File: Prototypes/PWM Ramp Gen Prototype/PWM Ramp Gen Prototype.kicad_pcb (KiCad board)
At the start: 2 copper layers, 115 parts, among them J1 Conn_01x03, J2 Conn_01x03, J3 Conn_01x10, U1 HFBR-2521Z, U10 BD50FC0FP-E2, U11 BD50FC0FP-E2, U12 BD33FC0FP-E2, U13 REF3433TIDBVR, U2 AFBR-1528CZ, U3 74LVC1G97, U4 74LVC1G97, U5 74LV1T04, U6 LT6230, U7 TLV3502, U8 74LVC1G97, U9 AD8602

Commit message: Finishing layout
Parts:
- added kibuzzard-65FA71D7: G***, kibuzzard-65FA71D7, B.Cu at (145.7, 43.4)
- added kibuzzard-65FA722F: G***, kibuzzard-65FA722F, B.Cu at (150.2, 48.5)
- added kibuzzard-65FA7252: G***, kibuzzard-65FA7252, B.Cu at (150.5, 84.8)
- moved TP27 137.6 mm to (108.0, 70.5)
- moved TP3 126.8 mm to (142.0, 57.5)
- moved TP31 121.0 mm to (145.5, 41.5)
- moved TP36 118.6 mm to (152.5, 41.5)
- moved TP30 114.8 mm to (142.0, 54.5)
- moved TP33 111.6 mm to (142.0, 63.5)
- moved J3 104.2 mm to (162.5, 52.1)
- moved R16 34.8 mm to (145.5, 59.0)
- moved TP23 33.6 mm to (145.5, 56.0)
- moved TP22 32.8 mm to (148.5, 68.2)
- moved TP21 30.2 mm to (144.5, 68.2)
- moved R15 28.1 mm to (150.0, 61.5), turned to 90 degrees
- moved U8 27.6 mm to (146.5, 61.5), turned to 180 degrees
- moved R23 26.4 mm to (139.0, 57.5), turned to 90 degrees
- moved R14 26.3 mm to (145.5, 65.0), turned to 90 degrees
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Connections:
- U1 pad 6: unconnected-(U1-MNT-Pad5) -> unconnected-(U1-MNT-Pad6)
- U2 pad 6: unconnected-(U2-MNT-Pad5) -> unconnected-(U2-MNT-Pad6)
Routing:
- net /HALF_V_{REF}: track 0.00 -> 105.9 mm, vias 0 -> 3
- net /Integrator Ramp Generator/V_{SERVO}: track 0.00 -> 74.1 mm, vias 0 -> 2
- net /+5V_ANA: track 0.00 -> 72.5 mm, vias 0 -> 9
- net +3.3V: track 0.00 -> 71.7 mm, vias 0 -> 7
- net +5V: track 0.00 -> 65.7 mm, vias 0 -> 9
- net /RAMP: track 0.00 -> 44.8 mm, vias 0 -> 1
- net /PWM_MIN: track 0.00 -> 39.0 mm, vias 0 -> 1
- net /PWM_MAX: track 0.00 -> 37.0 mm, vias 0 -> 1
- net Net-(D1-K): track 0.00 -> 33.8 mm, vias 0 -> 2
- net /SQUARE_IN: track 0.00 -> 31.6 mm
- net /V_{IN}: track 0.00 -> 20.2 mm, vias 0 -> 1
- net Net-(U7A-+): track 0.00 -> 19.7 mm
- net V_{REF}: track 0.00 -> 19.5 mm, vias 0 -> 4
- net Net-(U7B-+): track 0.00 -> 17.5 mm
- net /Square Wave Input/Y: track 0.00 -> 16.3 mm
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- added copper zone on F.Cu, net +3.3V
- added copper zone on In2.Cu, net +3.3V
- added copper zone on F.Cu, net +5V
- added copper zone on In2.Cu, net +5V
- added copper zone on F.Cu, net /+5V_ANA
- added copper zone on In2.Cu, net /+5V_ANA
- added copper zone on B.Cu, net GND
- added copper zone on F.Cu, net GND
- added copper zone on In1.Cu, net GND
- added copper zone on F.Cu, net Net-(D2-K)
- added copper zone on F.Cu, net Net-(D3-K)
- added copper zone on F.Cu, net Net-(U13-VDD)
- added copper zone on In2.Cu, net V_{REF}
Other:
- board outline added: 67 x 52 mm
- copper layers 2 -> 4
- rule pad_to_mask_clearance: 0 -> 0.0381
- board text added: "+3.3V_{D}"
- board text added: "+5V_{ANA}"
- board text added: "+5V_{D}"
- board text added: "PWM_MAX"
- board text added: "PWM_MIN"
- board text added: "RAMP"
- board text added: "V_{REF}"
- board text added: "V_{REF}/2"

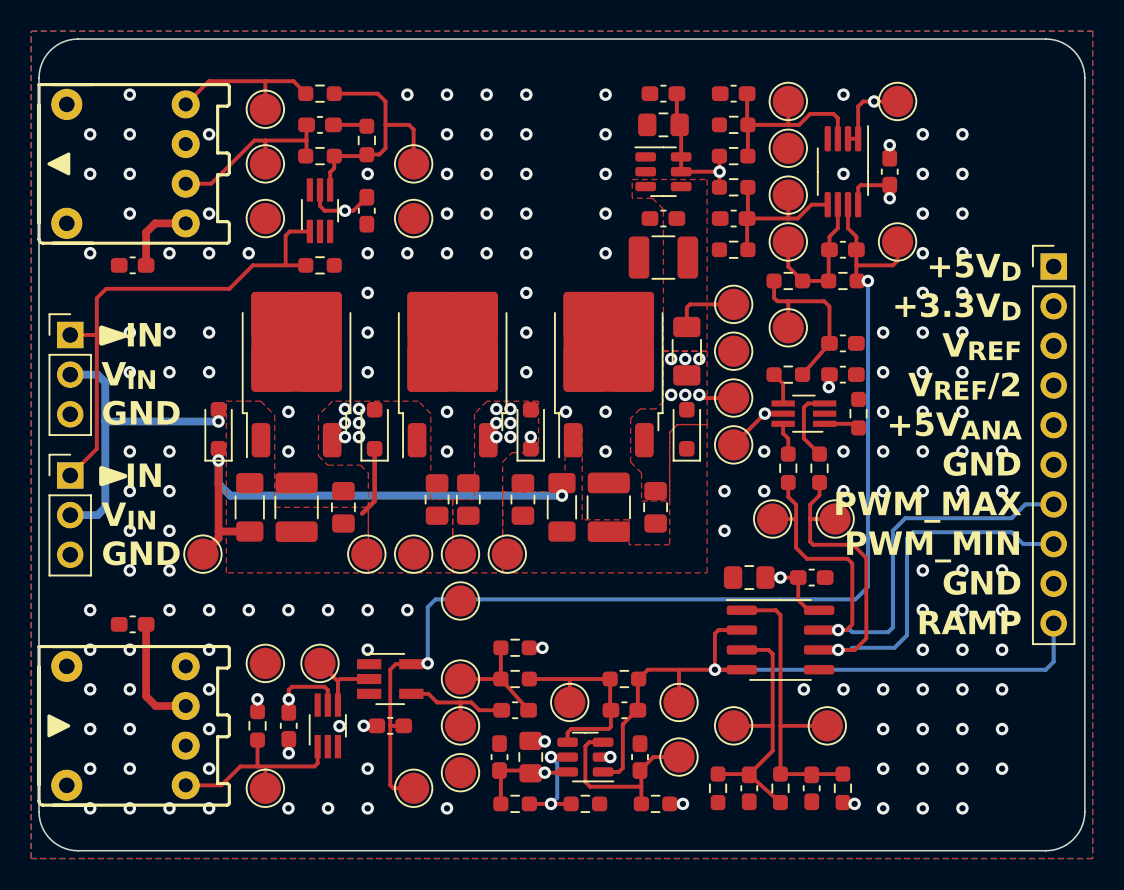
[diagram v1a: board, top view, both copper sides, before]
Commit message: Comparator and Op-amp tweaks for BOM consolidation; final layout
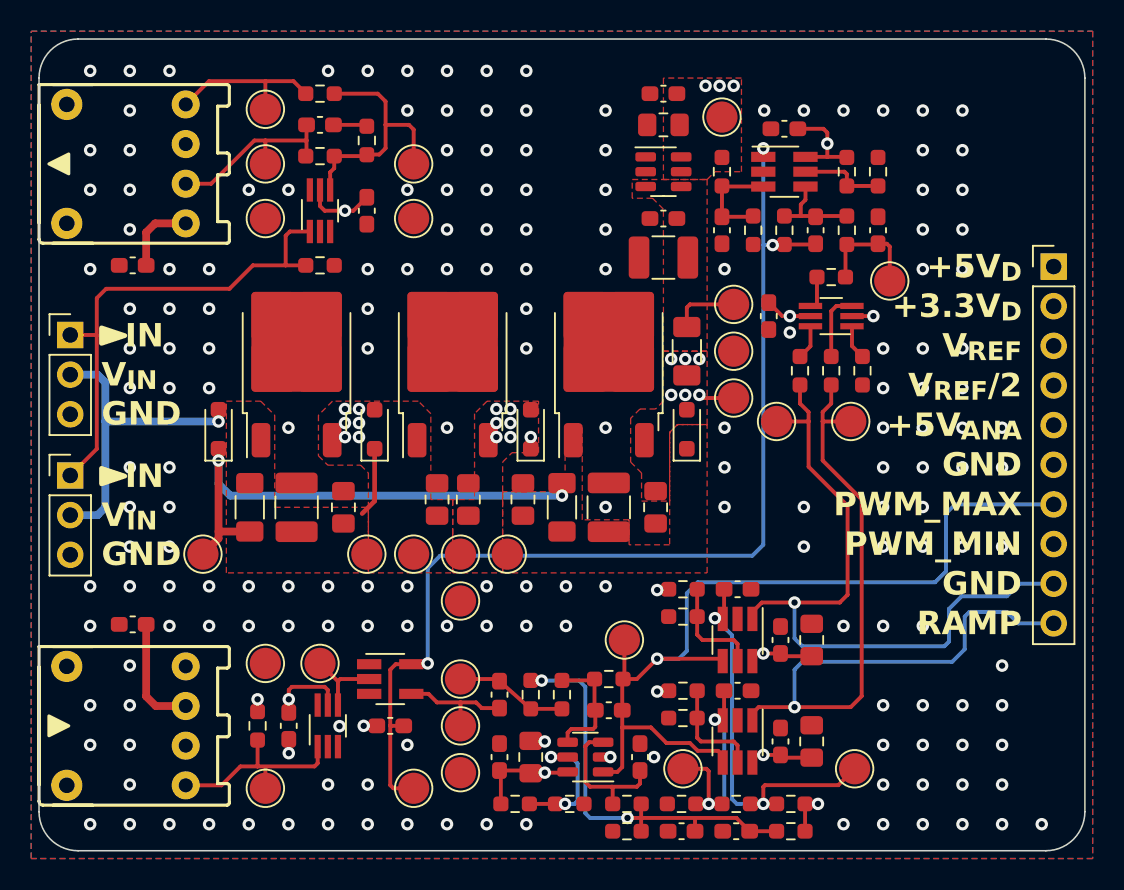
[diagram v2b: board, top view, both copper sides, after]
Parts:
- removed the C21 at (147.0, 72.0)
- removed the C22 at (143.0, 72.0)
- removed the C32 at (142.0, 41.0)
- removed the R26 at (142.0, 45.0)
- removed the TP16 at (131.5, 80.0)
- removed the TP17 at (138.5, 83.5)
- removed the TP24 at (145.5, 47.5)
- removed the TP25 at (145.5, 50.5)
- removed the TP26 at (152.5, 50.5)
- removed TP31, TP36, TP5: -, TestPoint:TestPoint_Pad_D2.0mm
- removed the U9 at (149.0, 46.0)
- added C10: 10n, Capacitor_SMD:C_0603_1608Metric_Pad1.08x0.95mm_HandSolder, F.Cu at (136.0, 83.5)
- added C23: 100n, Capacitor_SMD:C_0603_1608Metric_Pad1.08x0.95mm_HandSolder, F.Cu at (145.0, 76.0)
- added C24: 4.7u, Capacitor_SMD:C_0805_2012Metric_Pad1.18x1.45mm_HandSolder, F.Cu at (147.0, 76.0)
- added C30: 100n, Capacitor_SMD:C_0603_1608Metric_Pad1.08x0.95mm_HandSolder, F.Cu at (145.0, 82.5)
- added C31: 4.7u, Capacitor_SMD:C_0805_2012Metric_Pad1.18x1.45mm_HandSolder, F.Cu at (147.0, 82.5)
- added C7: 100n, Capacitor_SMD:C_0603_1608Metric_Pad1.08x0.95mm_HandSolder, F.Cu at (142.2, 88.2)
- added R23: 0R, Resistor_SMD:R_0603_1608Metric_Pad0.98x0.95mm_HandSolder, F.Cu at (149.2, 46.0)
- added R24: DNP, Custom-RLC:DNP_R_0603_1608Metric_Pad0.98x0.95mm_HandSolder, F.Cu at (151.2, 46.0)
- added R28: 0R, Resistor_SMD:R_0603_1608Metric_Pad0.98x0.95mm_HandSolder, F.Cu at (138.8, 74.5)
- added R30: DNP, Custom-RLC:DNP_R_0603_1608Metric_Pad0.98x0.95mm_HandSolder, F.Cu at (138.8, 79.2)
- added R31: 0R, Resistor_SMD:R_0603_1608Metric_Pad0.98x0.95mm_HandSolder, F.Cu at (138.8, 81.0)
- added R6: 1k 0.1%, Resistor_SMD:R_0603_1608Metric_Pad0.98x0.95mm_HandSolder, F.Cu at (145.7, 88.2)
- added R7: 1k 0.1%, Resistor_SMD:R_0603_1608Metric_Pad0.98x0.95mm_HandSolder, F.Cu at (135.2, 88.2)
- added U10: AD8601, Package_TO_SOT_SMD:SOT-23-6_Handsoldering, F.Cu at (145.2, 46.0)
- added U8: MAX9011EUT+T, Package_TO_SOT_SMD:SOT-23-6_Handsoldering, F.Cu at (142.2, 82.5)
- R27: value 4.7k -> DNP; footprint Resistor_SMD:R_0603_1608Metric_Pad0.98x0.95mm_HandSolder -> Custom-RLC:DNP_R_0603_1608Metric_Pad0.98x0.95mm_HandSolder
- U7: value TLV3502 -> MAX9011EUT+T; footprint Package_SO:SOIC-8_3.9x4.9mm_P1.27mm -> Package_TO_SOT_SMD:SOT-23-6_Handsoldering
- moved R27 29.9 mm to (138.8, 72.8), turned to 0 degrees
- moved TP27 21.0 mm to (141.2, 42.5)
- moved C12 13.6 mm to (142.2, 72.8), turned to 0 degrees
- moved C15 7.59 mm to (151.2, 49.8), turned to 90 degrees
- moved C18 7.29 mm to (145.2, 43.2), turned to 180 degrees
- moved TP21 7.16 mm to (152.0, 53.0)
- moved R18 6.83 mm to (148.2, 52.8)
- moved U9 6.49 mm to (148.2, 55.2)
- moved TP20 6.33 mm to (149.5, 62.0)
- moved C13 6.29 mm to (142.2, 79.2), turned to 0 degrees
- moved R15 6.29 mm to (148.2, 58.8)
- moved R16 6.29 mm to (146.2, 58.8)
- moved TP19 6.25 mm to (144.8, 62.0)
- moved C14 6.05 mm to (144.2, 55.2), turned to -90 degrees
- moved C8 5.45 mm to (138.7, 88.2), turned to 180 degrees
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- renumbered C9 to C11, C10 to C12, C11 to C13, C12 to C14, C13 to C15, C14 to C16, C15 to C17, C16 to C18, C17 to C19, C18 to C20, C19 to C21, C20 to C22, C23 to C25, C24 to C26, C30 to C32, C31 to C33, C25 to C34, C26 to C35, C7 to C9, R8 to R10, R9 to R11, R10 to R12, R11 to R13, R12 to R14, R13 to R15, R14 to R16, R15 to R17, R16 to R18, R17 to R19, R18 to R20, R19 to R21, R20 to R22, R21 to R25, R22 to R26, R23 to R29, R24 to R32, R25 to R33, R6 to R8, R7 to R9, TP18 to TP16, TP19 to TP17, TP20 to TP18, TP21 to TP19, TP22 to TP20, TP23 to TP21, TP27 to TP22, TP28 to TP23, TP29 to TP24, TP30 to TP25, TP32 to TP26, TP33 to TP27, TP34 to TP28, TP35 to TP29, U10 to U11, U11 to U12, U12 to U13, U13 to U14, U8 to U9
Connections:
- C13 pad 1: Net-(U7B-+) -> Net-(U8A-+)
- C8 pad 1: Net-(C8-Pad1) -> Net-(C7-Pad1)
- J3 pad 10: /RAMP -> /PWM_MIN
- J3 pad 3: V_{REF} -> GND
- J3 pad 4: /HALF_V_{REF} -> V_{REF}
- J3 pad 7: /PWM_MAX -> /RAMP
- J3 pad 8: /PWM_MIN -> GND
- J3 pad 9: GND -> /PWM_MAX
- R10 pad 1: /HALF_V_{REF} -> Net-(C7-Pad1)
- R10 pad 2: Net-(C8-Pad1) -> Net-(C10-Pad1)
- R13 pad 2: Net-(U7B-+) -> Net-(U8A-+)
- R14 pad 1: Net-(U7B-+) -> Net-(U8A-+)
- R27 pad 1: Net-(U9A-+) -> /+5V_ANA
- R27 pad 2: GND -> Net-(U7B-LATCH)
- R8 pad 2: /HALF_V_{REF} -> Net-(C7-Pad1)
- TP18 pad 1: Net-(U7B-+) -> Net-(U8A-+)
- U6 pad 3: Net-(C8-Pad1) -> Net-(C10-Pad1)
- U7 pad 1: Net-(U7A-+) -> /PWM_MAX
- U7 pad 2: /RAMP -> GND
- U7 pad 3: Net-(U7B-+) -> Net-(U7A-+)
- U7 pad 5: GND -> Net-(U7B-LATCH)
- U7 pad 6: /PWM_MIN -> /+5V_ANA
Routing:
- net /HALF_V_{REF}: track 105.9 -> 0.00 mm, vias 3 -> 0
- net V_{REF}: track 19.5 -> 101.2 mm, vias 4 -> 5
- net /+5V_ANA: track 72.5 -> 25.1 mm, vias 9 -> 12
- net Net-(C7-Pad1): track 0.00 -> 26.4 mm, vias 0 -> 2
- net Net-(U7B-+): track 17.5 -> 0.00 mm
- net Net-(U8A-+): track 0.00 -> 14.4 mm, vias 0 -> 2
- net /PWM_MIN: track 39.0 -> 53.0 mm
- net /RAMP: track 44.8 -> 57.9 mm
- net Net-(U9A-+): track 12.9 -> 0.00 mm
- net Net-(C8-Pad1): track 12.2 -> 0.00 mm
- net Net-(C10-Pad1): track 0.00 -> 9.21 mm
- net /PWM_MAX: track 37.0 -> 45.8 mm
- net Net-(U8B-LATCH): track 0.00 -> 6.90 mm
- net Net-(U7B-LATCH): track 0.00 -> 6.84 mm
- net Net-(U7A-+): track 19.7 -> 25.7 mm, vias 0 -> 2
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- added copper zone on F.Cu, net V_{REF}
- removed copper zone on In2.Cu, net V_{REF}
